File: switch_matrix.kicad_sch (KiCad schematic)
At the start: 136 parts

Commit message: Added 3d models to footprints and updated partnumbers
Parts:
- MX1, MX10, MX11, MX12, MX13, MX14, MX15, MX16, MX18, MX19, MX2, MX20, MX21, MX22, MX23, MX24, MX25, MX26, MX27, MX28, MX29, MX3, MX33, MX34, MX35, MX36, MX37, MX38, MX39, MX4, MX40, MX41, MX42, MX43, MX46, MX47, MX48, MX49, MX5, MX50, MX51, MX52, MX53, MX54, MX55, MX57, MX58, MX6, MX7, MX72, MX73, MX8, MX9: footprint (none) -> keyboard:SW_Cherry_MX_1.00u_PCB
- MX17, MX30, MX62, MX63, MX64, MX71: footprint (none) -> keyboard:SW_Cherry_MX_1.50u_PCB
- MX31, MX56: footprint (none) -> keyboard:SW_Cherry_MX_1.75u_PCB
- MX32, MX59, MX60, MX61, MX67, MX68, MX69, MX70: footprint (none) -> keyboard:SW_Cherry_MX_1.25u_PCB
- MX44, MX45: footprint (none) -> keyboard:SW_Cherry_MX_2.25u_PCB
- MX65: footprint (none) -> keyboard:SW_Cherry_MX_6.25u_PCB
- MX66: footprint (none) -> keyboard:SW_Cherry_MX_7.00u_PCB

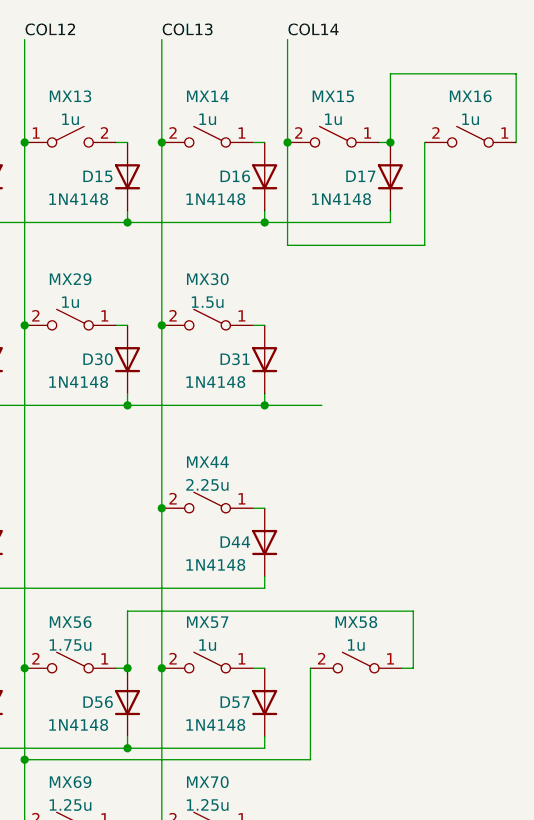
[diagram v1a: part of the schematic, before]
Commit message: Placed switches
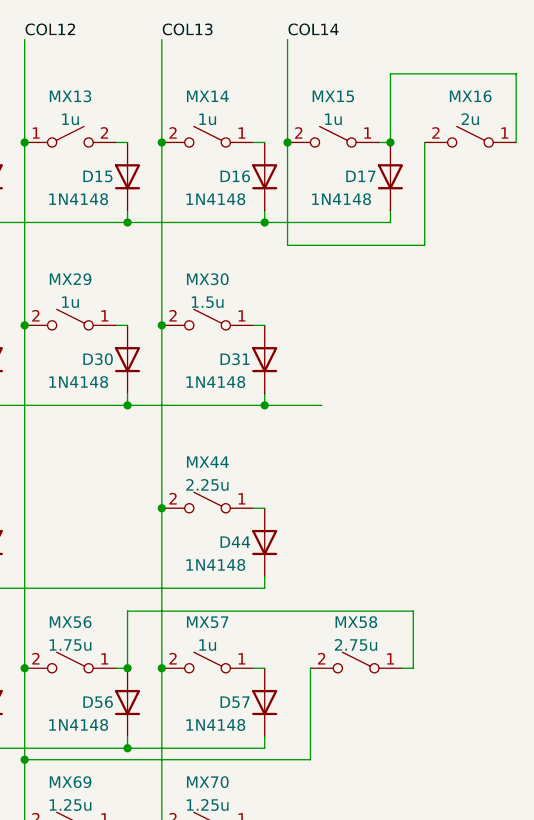
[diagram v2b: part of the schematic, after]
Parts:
- MX16: value 1u -> 2u; footprint keyboard:SW_Cherry_MX_1.00u_PCB -> keyboard:SW_Cherry_MX_2.00u_PCB
- MX58: value 1u -> 2.75u; footprint keyboard:SW_Cherry_MX_1.00u_PCB -> keyboard:SW_Cherry_MX_2.75u_PCB
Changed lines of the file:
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@@
       (effects (font (size 1.27 1.27)))
     )
-    (property "Value" "1u" (at 255.27 93.98 0)
-      (effects (font (size 1.27 1.27)))
-    )
-    (property "Footprint" "keyboard:SW_Cherry_MX_1.00u_PCB" (at 255.27 96.52 0)
+    (property "Value" "2.75u" (at 255.27 93.98 0)
+      (effects (font (size 1.27 1.27)))
+    )
+    (property "Footprint" "keyboard:SW_Cherry_MX_2.75u_PCB" (at 255.27 96.52 0)
       (effects (font (size 1.27 1.27)) hide)
     )
@@
       (effects (font (size 1.27 1.27)))
     )
-    (property "Value" "1u" (at 267.97 35.56 0)
-      (effects (font (size 1.27 1.27)))
-    )
-    (property "Footprint" "keyboard:SW_Cherry_MX_1.00u_PCB" (at 267.97 38.1 0)
-      (effects (font (size 1.27 1.27)) hide)
-    )
+    (property "Value" "2u" (at 267.97 35.56 0)
+      (effects (font (size 1.27 1.27)))
+    )
+    (property "Footprint" "keyboard:SW_Cherry_MX_2.00u_PCB" (at 267.97 38.1 0)
+      (effects (font (size 1.27 1.27)) hide)
+    )

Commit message: Pcb routing complete
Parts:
- D10, D11, D12, D13, D14, D15, D16, D17, D18, D19, D20, D21, D22, D23, D24, D25, D26, D27, D28, D29, D3, D30, D31, D32, D33, D34, D35, D36, D37, D38, D39, D4, D40, D41, D42, D43, D44, D45, D46, D47, D48, D49, D5, D50, D51, D52, D53, D54, D55, D56, D57, D58, D59, D6, D60, D61, D62, D63, D64, D65, D7, D8, D9: footprint Diode_THT:D_DO-35_SOD27_P7.62mm_Horizontal -> keyboard:D_SOD-123; LCSC Part Number (none) -> C391324; LCSC link (none) -> https://www.lcsc.com/product-detail/Diodes-General-Purpose_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; PN (none) -> 1N4148W_R1_00001
- renumbered MX65 to MX62, MX67 to MX63, MX68 to MX64, MX69 to MX65, MX70 to MX66, MX62 to MX67, MX63 to MX68, MX64 to MX69, MX66 to MX70
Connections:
- net COL12: now also MX13.2 (B); no longer MX13.1 (A)
- net ROW2: now also D35.1 (K)
- net at D15.2 (A): now also MX13.1 (A); no longer MX13.2 (B)

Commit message: Completed routing and solved DRC
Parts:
- MX68: value 1.5u -> 1u; footprint keyboard:SW_Cherry_MX_1.50u_PCB -> keyboard:SW_Cherry_MX_1.00u_PCB
- MX73: footprint keyboard:SW_Cherry_MX_1.00u_PCB -> keyboard:SW_Cherry_MX_1.50u_PCB
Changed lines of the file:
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@@
       (effects (font (size 1.27 1.27)))
     )
-    (property "Footprint" "keyboard:SW_Cherry_MX_1.00u_PCB" (at 238.76 130.81 0)
+    (property "Footprint" "keyboard:SW_Cherry_MX_1.50u_PCB" (at 238.76 130.81 0)
       (effects (font (size 1.27 1.27)) hide)
     )
@@
       (effects (font (size 1.27 1.27)))
     )
-    (property "Value" "1.5u" (at 57.15 128.27 0)
-      (effects (font (size 1.27 1.27)))
-    )
-    (property "Footprint" "keyboard:SW_Cherry_MX_1.50u_PCB" (at 57.15 130.81 0)
-      (effects (font (size 1.27 1.27)) hide)
-    )
+    (property "Value" "1u" (at 57.15 128.27 0)
+      (effects (font (size 1.27 1.27)))
+    )
+    (property "Footprint" "keyboard:SW_Cherry_MX_1.00u_PCB" (at 57.15 130.81 0)
+      (effects (font (size 1.27 1.27)) hide)
+    )

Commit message: gerber generated
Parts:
- D10, D11, D12, D13, D14, D15, D16, D17, D18, D19, D20, D21, D22, D23, D24, D25, D26, D27, D28, D29, D3, D30, D31, D32, D33, D34, D35, D36, D37, D38, D39, D4, D40, D41, D42, D43, D44, D45, D46, D47, D48, D49, D5, D50, D51, D52, D53, D54, D55, D56, D57, D58, D59, D6, D60, D61, D62, D63, D64, D65, D7, D8, D9: value 1N4148 -> 1N4148W; LCSC Part Number C391324 -> C81598; LCSC link https://www.lcsc.com/product-detail/Diodes-General-Purpose_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 -> https://www.lcsc.com/product-detail/Switching-Diode_ST-Semt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; PN 1N4148W_R1_00001 -> 1N4148W
- MX73: value 1u -> 1.5u
